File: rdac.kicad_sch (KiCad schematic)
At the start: 18 parts

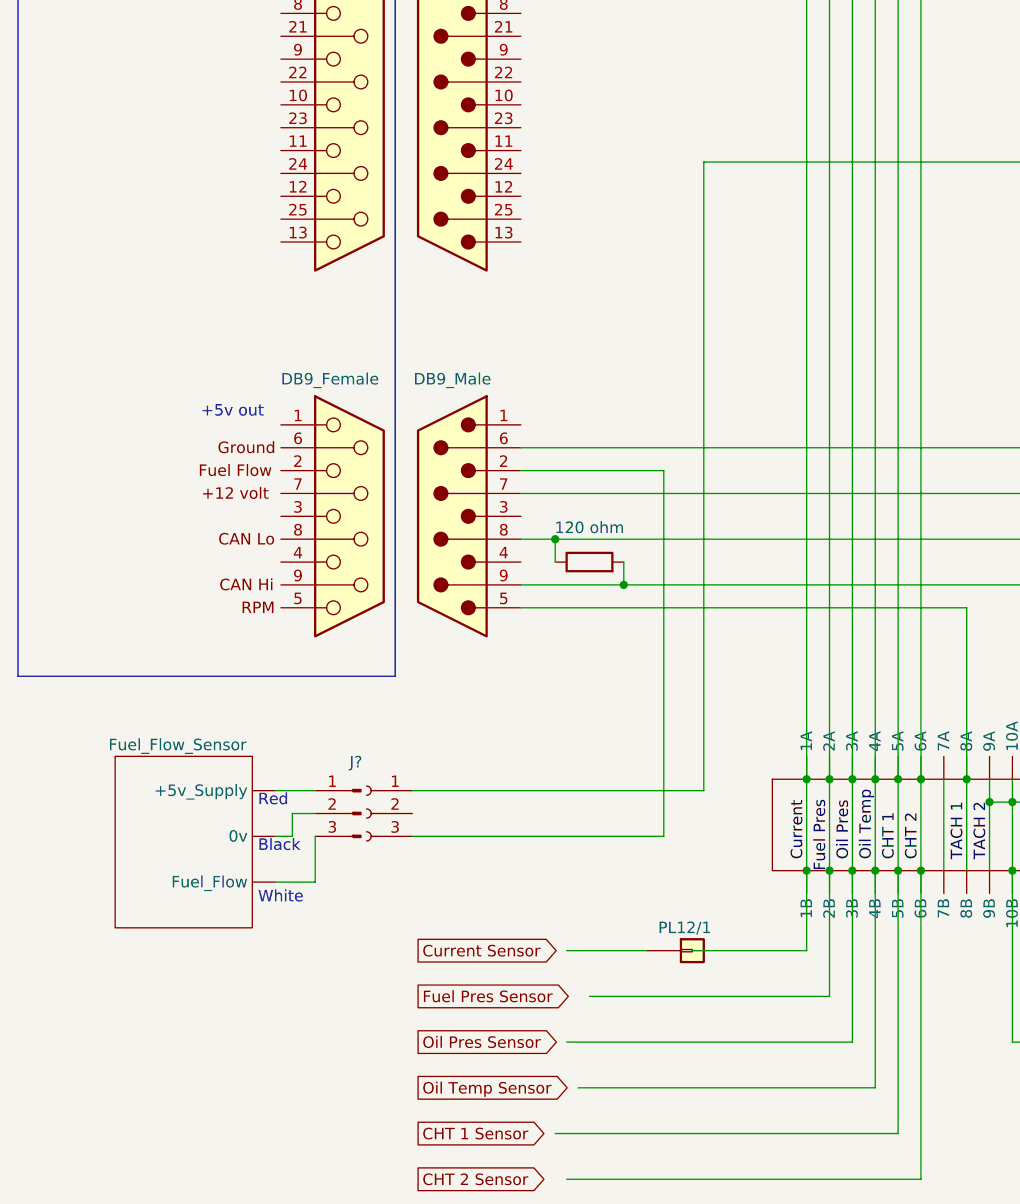
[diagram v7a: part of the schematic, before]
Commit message: Added PL20 to COM Sheet
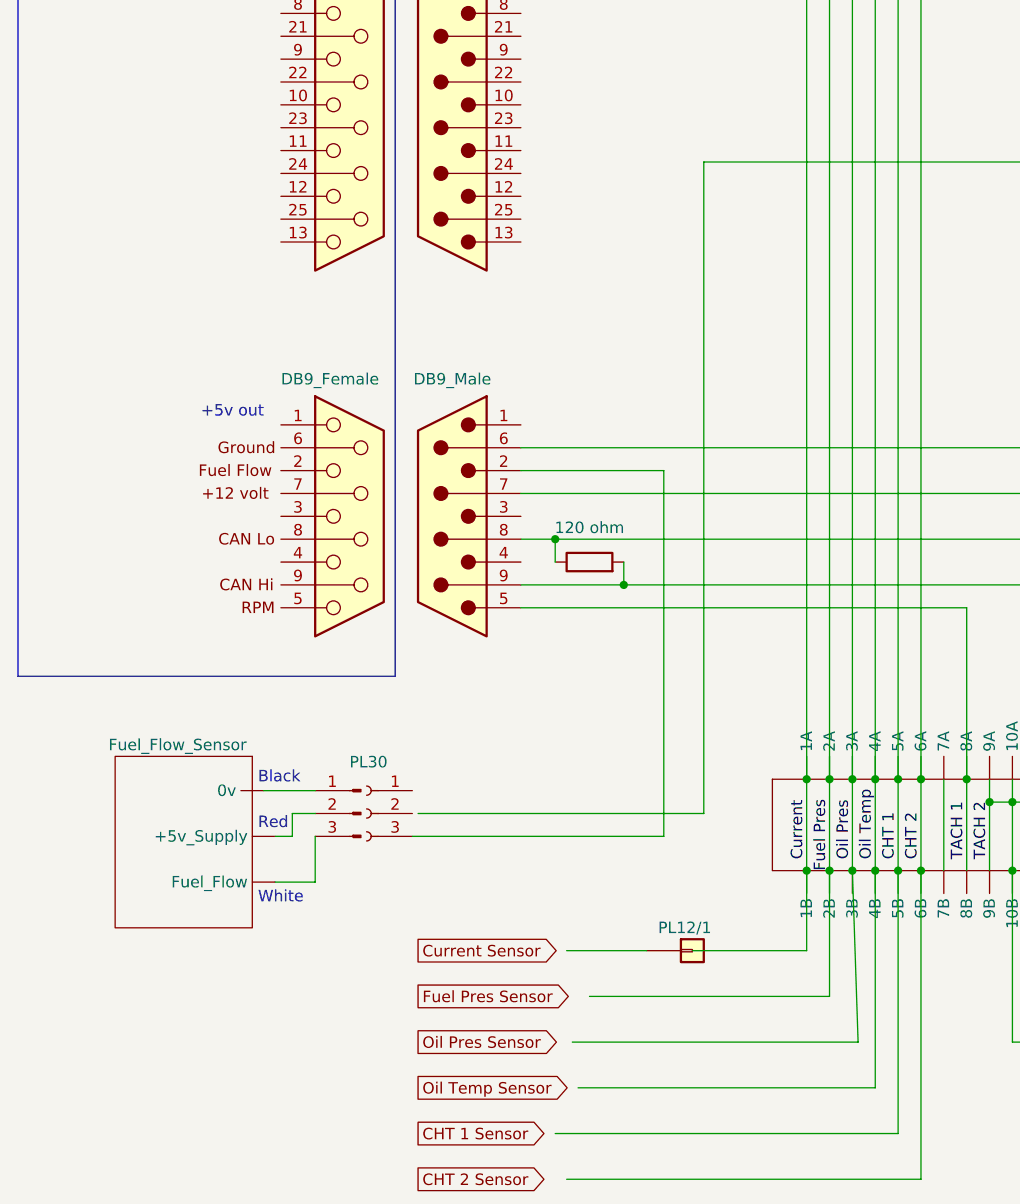
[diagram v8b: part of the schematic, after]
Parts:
- gave numbers to parts that had none: 1
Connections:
- net at FB2/2.1: no longer J?.1 (Pin_1)
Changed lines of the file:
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@@
     (stroke (width 0) (type default) (color 0 0 0 0))
   )
-  (wire (pts (xy 114.3 157.48) (xy 114.3 176.53))
+  (wire (pts (xy 114.3 157.48) (xy 114.935 176.53))
     (stroke (width 0) (type default) (color 0 0 0 0))
   )
@@
     (stroke (width 0) (type default) (color 0 0 0 0))
   )
+  (wire (pts (xy 48.895 148.59) (xy 54.61 148.59))
+    (stroke (width 0) (type default) (color 0 0 0 0))
+  )
   (wire (pts (xy 124.46 147.32) (xy 124.46 157.48))
     (stroke (width 0) (type dot) (color 0 0 0 0))
@@
     (stroke (width 0) (type default) (color 0 0 0 0))
   )
-  (wire (pts (xy 97.79 148.59) (xy 97.79 78.74))
-    (stroke (width 0) (type default) (color 0 0 0 0))
-  )
   (wire (pts (xy 228.6 86.36) (xy 222.25 86.36))
     (stroke (width 0) (type default) (color 0 0 0 0))
@@
     (stroke (width 0) (type default) (color 0 0 0 0))
   )
-  (wire (pts (xy 50.165 148.59) (xy 54.61 148.59))
-    (stroke (width 0) (type default) (color 0 0 0 0))
-  )
   (wire (pts (xy 77.47 110.49) (xy 137.16 110.49))
     (stroke (width 0) (type default) (color 0 0 0 0))
@@
     (stroke (width 0) (type default) (color 0 0 0 0))
   )
-  (wire (pts (xy 82.55 176.53) (xy 114.3 176.53))
+  (wire (pts (xy 83.185 176.53) (xy 114.935 176.53))
     (stroke (width 0) (type default) (color 0 0 0 0))
   )
@@
     (stroke (width 0) (type default) (color 0 0 0 0))
   )
-  (wire (pts (xy 65.405 148.59) (xy 97.79 148.59))
-    (stroke (width 0) (type default) (color 0 0 0 0))
-  )
   (wire (pts (xy 88.9 125.73) (xy 147.32 125.73))
     (stroke (width 0) (type default) (color 0 0 0 0))
@@
     (stroke (width 0) (type default) (color 0 0 0 0))
   )
+  (wire (pts (xy 66.04 151.13) (xy 97.79 151.13))
+    (stroke (width 0) (type default) (color 0 0 0 0))
+  )
   (wire (pts (xy 85.09 171.45) (xy 111.76 171.45))
     (stroke (width 0) (type default) (color 0 0 0 0))
@@
     (stroke (width 0) (type default) (color 0 0 0 0))
   )
+  (wire (pts (xy 97.79 151.13) (xy 97.79 78.74))
+    (stroke (width 0) (type default) (color 0 0 0 0))
+  )
   (text "+5v out" (at 41.91 107.315 0)
     (effects (font (size 1.27 1.27)) (justify left bottom))
@@
     (effects (font (size 1.27 1.27)) (justify left bottom))
   )
-  (text "Black" (at 48.26 155.575 0)
+  (text "Black" (at 48.26 147.955 0)
     (effects (font (size 1.27 1.27)) (justify left bottom))
   )
@@
     (effects (font (size 1.27 1.27)) (justify left bottom))
   )
-  (text "Red" (at 48.26 150.495 0)
+  (text "Red" (at 48.26 153.035 0)
     (effects (font (size 1.27 1.27)) (justify left bottom))
   )
@@
   (symbol (lib_id "Connector:Conn_01x03_Male") (at 59.69 151.13 0) (mirror y) (unit 1)
     (in_bom yes) (on_board yes)
-    (property "Reference" "J?" (id 0) (at 58.42 145.415 0)
+    (property "Reference" "PL30" (id 0) (at 58.42 145.415 0)
       (effects (font (size 1.27 1.27)) (justify right))
     )
